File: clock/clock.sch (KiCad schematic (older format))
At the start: 21 parts

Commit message: Selected to use the LPC804 over the PIC18F45k20
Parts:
- removed U?: PIC18F45K50_QFP, Package_QFP:TQFP-44_10x10mm_P0.8mm, symbol MCU_Microchip_PIC18:PIC18F45K50_QFP
- added D? (x72): LED, symbol Device:LED
- added R? (x72): 0, symbol Device:R_Small_US
- added U?: LPC804-TSSOP24, symbol MCU_NXP_LPC804:LPC804-TSSOP24
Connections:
- net labels added: GND, ~OE
- wire segments 17 -> 110
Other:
- note added: "Shift Register"
- note removed: "Almost the correct processor"
- note removed: "Shift Register (Add LEDs)"

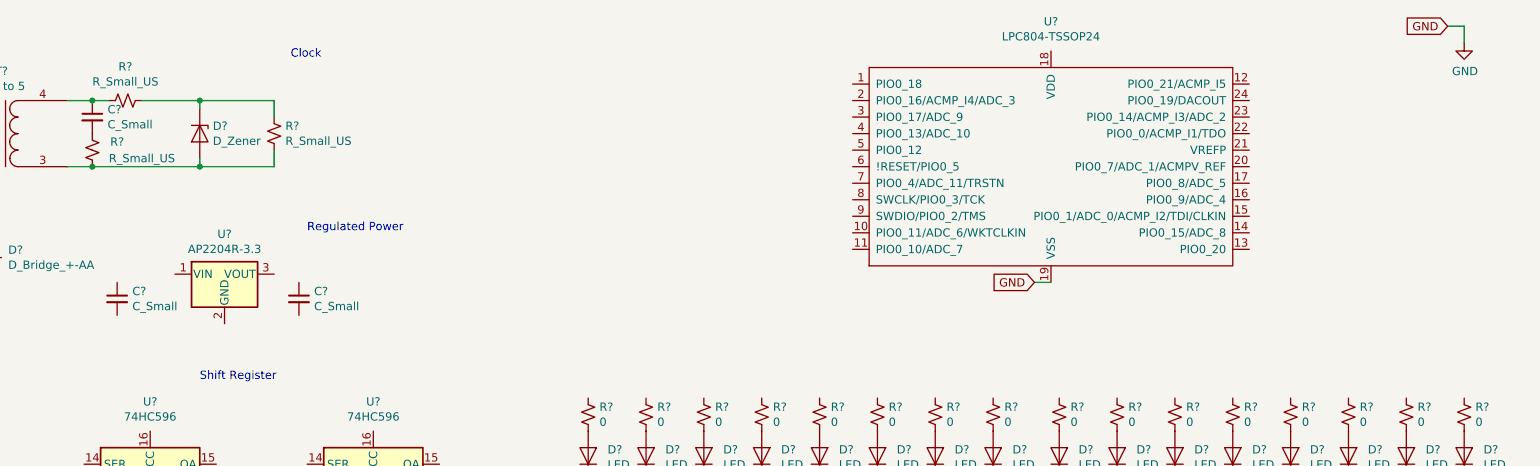
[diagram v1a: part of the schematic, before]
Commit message: Selecting serial data lines impressed the importance of selecting appropriate pins for my cap touch
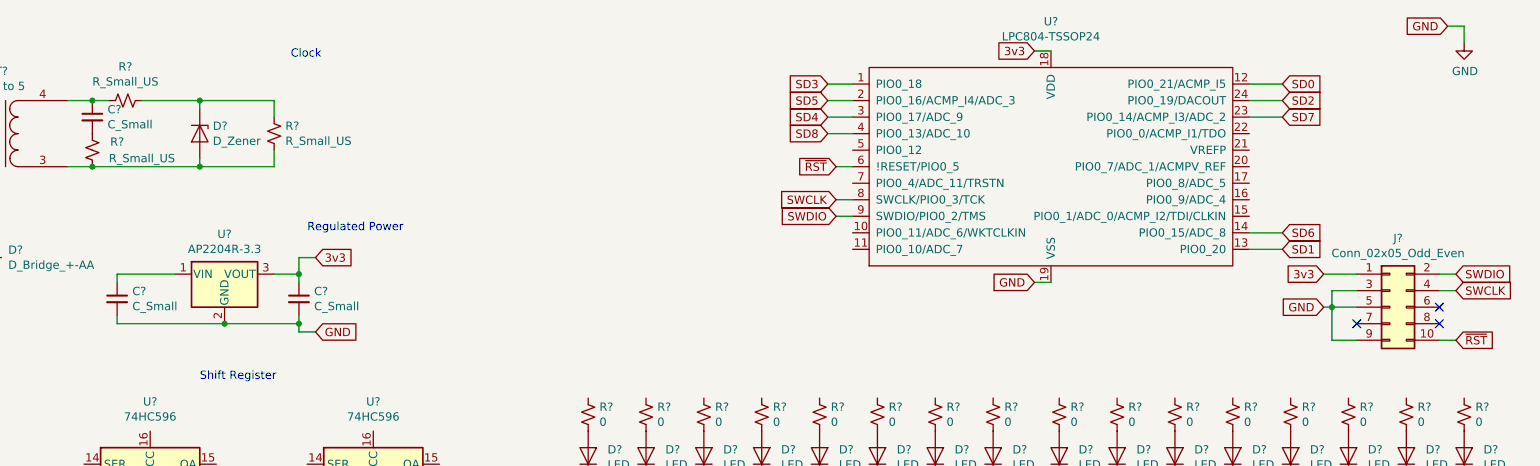
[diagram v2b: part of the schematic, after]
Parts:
- added J?: Conn_02x05_Odd_Even, symbol Connector_Generic:Conn_02x05_Odd_Even
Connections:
- net GND: now also C?.2, C?.2, U?.2 (GND), J?.3 (Pin_3), J?.5 (Pin_5), J?.9 (Pin_9)
- net at U?.1 (VIN): now also C?.1
- net 3v3: now reaches U?.3 (VOUT)
- net 3v3: now also C?.1, U?.18 (VDD), J?.1 (Pin_1)
- net SD3: now reaches U?.1 (PIO0_18)
- net SD0: now reaches U?.12 (PIO0_21/ACMP_I5)
- net SD1: now reaches U?.13 (PIO0_20)
- net SD6: now reaches U?.14 (PIO0_15/ADC_8)
- net SD5: now reaches U?.2 (PIO0_16/ACMP_I4/ADC_3)
- net SD7: now reaches U?.23 (PIO0_14/ACMP_I3/ADC_2)
- net SD2: now reaches U?.24 (PIO0_19/DACOUT)
- net SD4: now reaches U?.3 (PIO0_17/ADC_9)
- net SD8: now reaches U?.4 (PIO0_13/ADC_10)
- net ~RST: now reaches U?.6 (!RESET/PIO0_5)
- net ~RST: now also J?.10 (Pin_10)
- net SWCLK: now reaches U?.8 (SWCLK/PIO0_3/TCK)
- net SWCLK: now also J?.4 (Pin_4)
- net SWDIO: now reaches U?.9 (SWDIO/PIO0_2/TMS)
- net SWDIO: now also J?.2 (Pin_2)
- no-connect marks 0 -> 3
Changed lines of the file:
@@
 Wire Wire Line
 	8350 2150 8450 2150
+$Comp
+L Connector_Generic:Conn_02x05_Odd_Even J?
+U 1 1 5E00183C
+P 10500 2300
+F 0 "J?" H 10550 2717 50  0000 C CNN
+F 1 "Conn_02x05_Odd_Even" H 10550 2626 50  0000 C CNN
+F 2 "" H 10500 2300 50  0001 C CNN
+F 3 "~" H 10500 2300 50  0001 C CNN
+	1    10500 2300
+	1    0    0    -1
+$EndComp
+Text GLabel 10100 2100 0    50   Input ~ 0
+3v3
+Wire Wire Line
+	10100 2100 10300 2100
+Text GLabel 10100 2300 0    50   Input ~ 0
+GND
+Wire Wire Line
+	10300 2200 10150 2200
+Wire Wire Line
+	10150 2200 10150 2300
+Wire Wire Line
+	10150 2300 10100 2300
+Wire Wire Line
+	10300 2300 10150 2300
+Connection ~ 10150 2300
+Wire Wire Line
+	10300 2500 10150 2500
+Wire Wire Line
+	10150 2500 10150 2300
+NoConn ~ 10300 2400
+NoConn ~ 10800 2400
+NoConn ~ 10800 2300
+Text GLabel 10900 2500 2    50   Input ~ 0
+~RST
+Text GLabel 10900 2200 2    50   Input ~ 0
+SWCLK
+Text GLabel 10900 2100 2    50   Input ~ 0
+SWDIO
+Wire Wire Line
+	10800 2100 10900 2100
+Wire Wire Line
+	10800 2200 10900 2200
+Wire Wire Line
+	10800 2500 10900 2500
+Text GLabel 7150 1750 0    50   Input ~ 0
+SWDIO
+Text GLabel 7150 1650 0    50   Input ~ 0
+SWCLK
+Wire Wire Line
+	7150 1650 7250 1650
+Wire Wire Line
+	7150 1750 7250 1750
+Text GLabel 7150 1450 0    50   Input ~ 0
+~RST
+Wire Wire Line
+	7150 1450 7250 1450
+Text GLabel 8350 750  0    50   Input ~ 0
+3v3
+Wire Wire Line
+	8350 750  8450 750
+Wire Wire Line
+	3750 2100 3900 2100
+Wire Wire Line
+	3900 2100 3900 2150
+Wire Wire Line
+	2800 2150 2800 2100
+Wire Wire Line
+	2800 2100 3150 2100
+Wire Wire Line
+	2800 2350 2800 2400
+Wire Wire Line
+	2800 2400 3450 2400
+Wire Wire Line
+	3900 2400 3900 2350
+Connection ~ 3450 2400
+Wire Wire Line
+	3450 2400 3900 2400
+Text GLabel 4000 2000 2    50   Input ~ 0
+3v3
+Text GLabel 4000 2450 2    50   Input ~ 0
+GND
+Wire Wire Line
+	4000 2000 3900 2000
+Wire Wire Line
+	3900 2000 3900 2100
+Connection ~ 3900 2100
+Wire Wire Line
+	4000 2450 3900 2450
+Wire Wire Line
+	3900 2450 3900 2400
+Connection ~ 3900 2400
+Text GLabel 9850 950  2    50   Input ~ 0
+SD0
+Text GLabel 9850 1950 2    50   Input ~ 0
+SD1
+Text GLabel 9850 1050 2    50   Input ~ 0
+SD2
+Text GLabel 7100 950  0    50   Input ~ 0
+SD3
+Text GLabel 7100 1150 0    50   Input ~ 0
+SD4
+Text GLabel 7100 1050 0    50   Input ~ 0
+SD5
+Text GLabel 9850 1850 2    50   Input ~ 0
+SD6
+Text GLabel 9850 1150 2    50   Input ~ 0
+SD7
+Text GLabel 7100 1250 0    50   Input ~ 0
+SD8
+Wire Wire Line
+	9650 950  9850 950
+Wire Wire Line
+	9650 1050 9850 1050
+Wire Wire Line
+	9650 1150 9850 1150
+Wire Wire Line
+	9650 1850 9850 1850
+Wire Wire Line
+	9650 1950 9850 1950
+Wire Wire Line
+	7100 950  7250 950
+Wire Wire Line
+	7100 1050 7250 1050
+Wire Wire Line
+	7100 1150 7250 1150
+Wire Wire Line
+	7100 1250 7250 1250
 $EndSCHEMATC

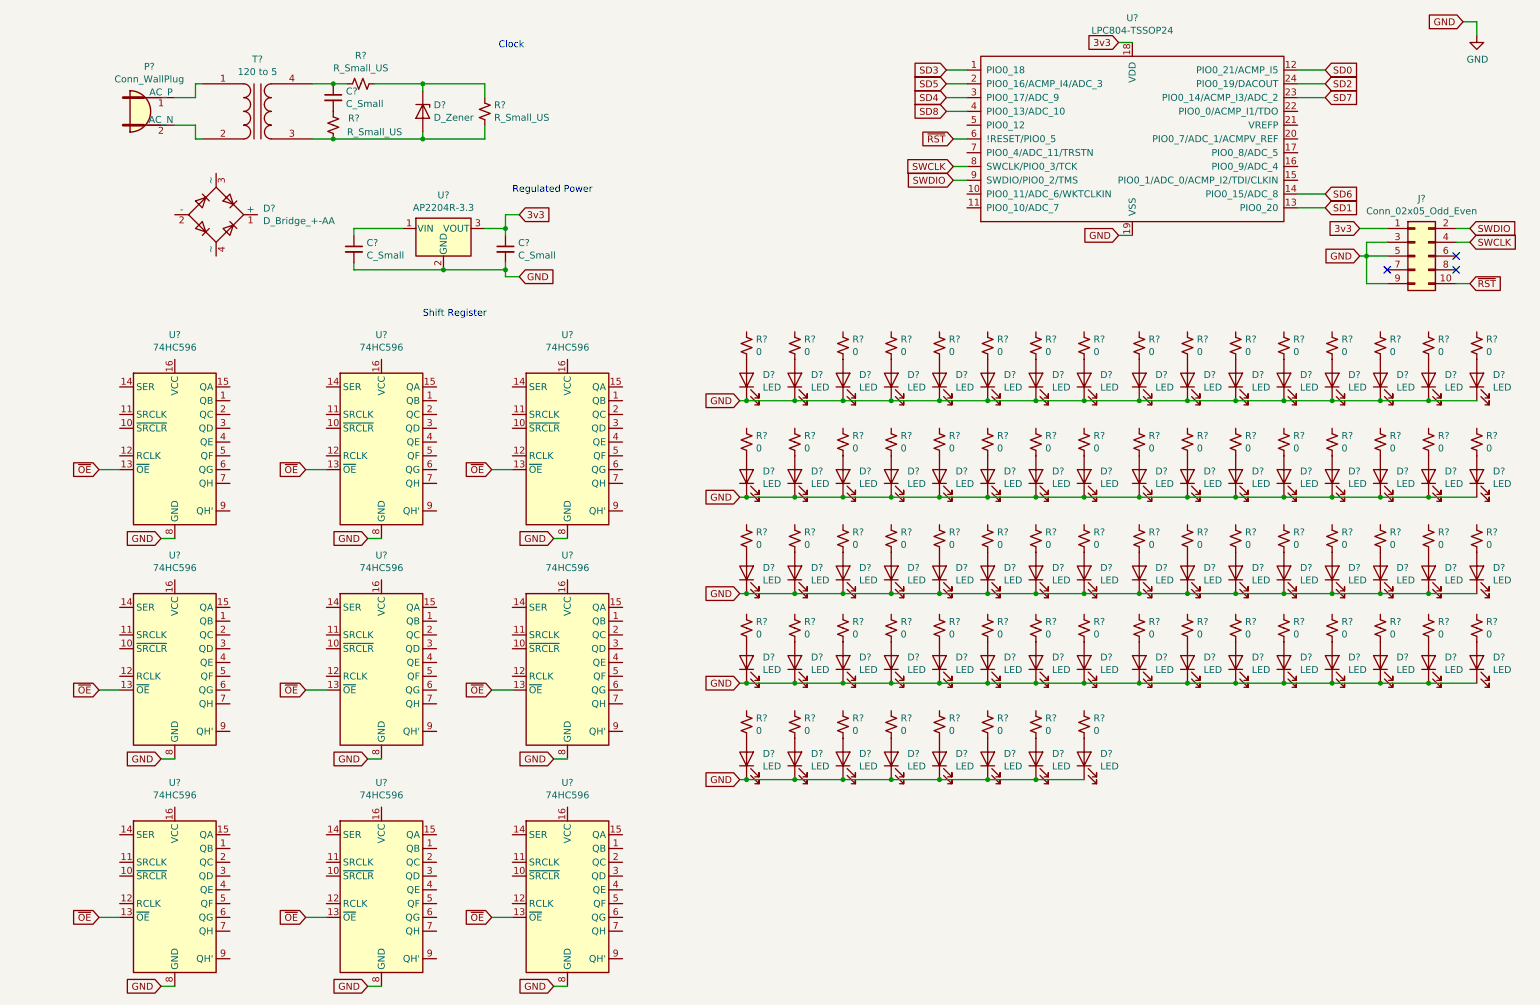
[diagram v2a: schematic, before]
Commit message: Selected 596 shift register. Redid LED schematics. Started bom. Updated readme todo list
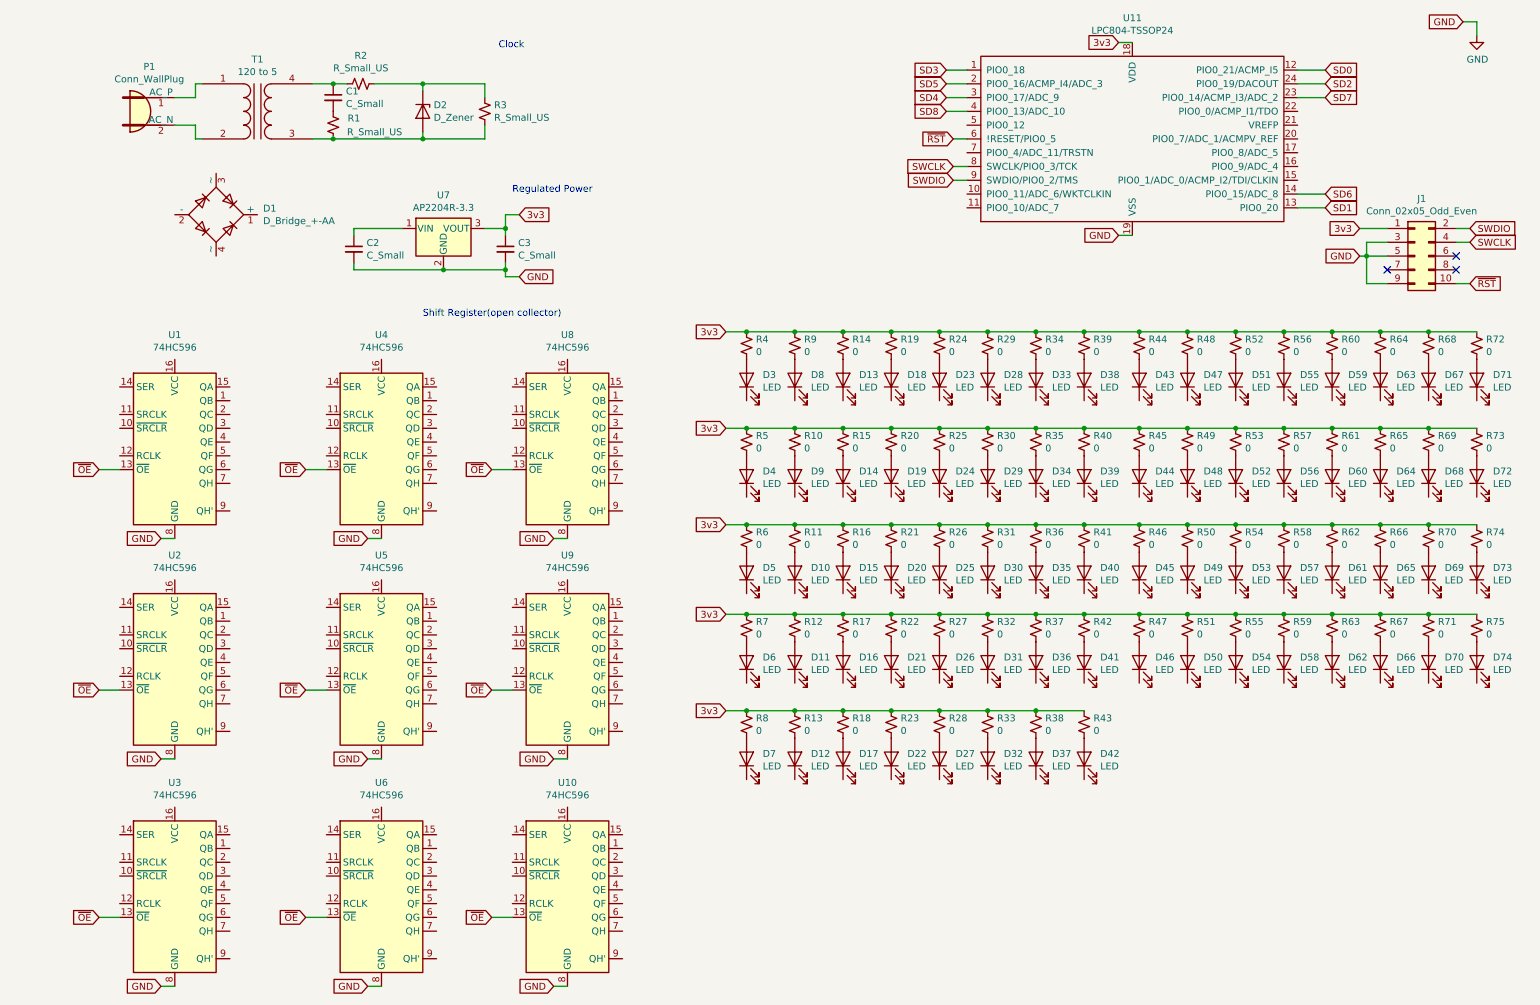
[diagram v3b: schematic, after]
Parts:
- gave numbers to parts that had none: 166
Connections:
- net 3v3: now also R10.1, R11.1, R12.1, R13.1, R14.1, R15.1, R16.1, R17.1, R18.1, R19.1, R20.1, R21.1, R22.1, R23.1, R24.1, R25.1, R26.1, R27.1, R28.1, R29.1, R30.1, R31.1, R32.1, R33.1, R34.1, R35.1, R36.1, R37.1, R38.1, R39.1, R4.1, R40.1, R41.1, R42.1, R43.1, R44.1, R45.1, R46.1, R47.1, R48.1, R49.1, R5.1, R50.1, R51.1, R52.1, R53.1, R54.1, R55.1, R56.1, R57.1, R58.1, R59.1, R6.1, R60.1, R61.1, R62.1, R63.1, R64.1, R65.1, R66.1, R67.1, R68.1, R69.1, R7.1, R70.1, R71.1, R72.1, R73.1, R74.1, R75.1, R8.1, R9.1
- net GND: no longer D10.1 (K), D11.1 (K), D12.1 (K), D13.1 (K), D14.1 (K), D15.1 (K), D16.1 (K), D17.1 (K), D18.1 (K), D19.1 (K), D20.1 (K), D21.1 (K), D22.1 (K), D23.1 (K), D24.1 (K), D25.1 (K), D26.1 (K), D27.1 (K), D28.1 (K), D29.1 (K), D3.1 (K), D30.1 (K), D31.1 (K), D32.1 (K), D33.1 (K), D34.1 (K), D35.1 (K), D36.1 (K), D37.1 (K), D38.1 (K), D39.1 (K), D4.1 (K), D40.1 (K), D41.1 (K), D42.1 (K), D43.1 (K), D44.1 (K), D45.1 (K), D46.1 (K), D47.1 (K), D48.1 (K), D49.1 (K), D5.1 (K), D50.1 (K), D51.1 (K), D52.1 (K), D53.1 (K), D54.1 (K), D55.1 (K), D56.1 (K), D57.1 (K), D58.1 (K), D59.1 (K), D6.1 (K), D60.1 (K), D61.1 (K), D62.1 (K), D63.1 (K), D64.1 (K), D65.1 (K), D66.1 (K), D67.1 (K), D68.1 (K), D69.1 (K), D7.1 (K), D70.1 (K), D71.1 (K), D72.1 (K), D73.1 (K), D74.1 (K), D8.1 (K), D9.1 (K)
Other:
- note added: "Shift Register(open collector)"
- note removed: "Shift Register"

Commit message: Worked on all LED and 596 nets before realizing that I was on the wrong branch. Going to push on branch 191311 and then switch my local back to the master branch
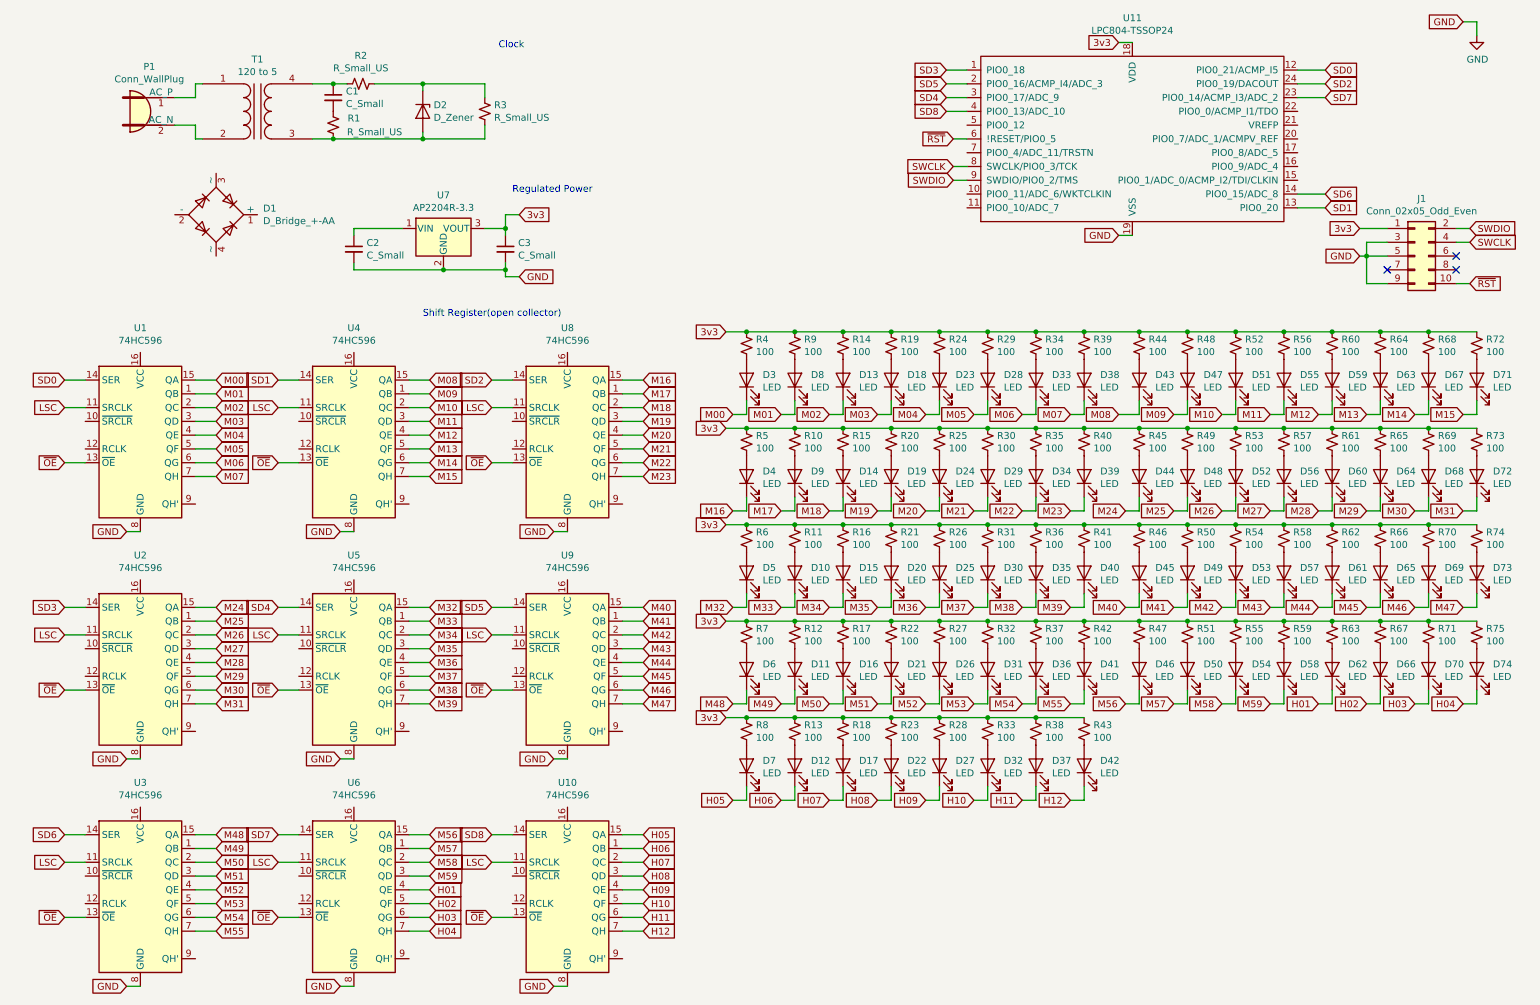
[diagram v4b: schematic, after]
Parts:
- R10, R11, R12, R13, R14, R15, R16, R17, R18, R19, R20, R21, R22, R23, R24, R25, R26, R27, R28, R29, R30, R31, R32, R33, R34, R35, R36, R37, R38, R39, R4, R40, R41, R42, R43, R44, R45, R46, R47, R48, R49, R5, R50, R51, R52, R53, R54, R55, R56, R57, R58, R59, R6, R60, R61, R62, R63, R64, R65, R66, R67, R68, R69, R7, R70, R71, R72, R73, R74, R75, R8, R9: value 0 -> 100
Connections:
- net SD0: now also U1.14 (SER)
- net SD1: now also U4.14 (SER)
- net SD2: now also U8.14 (SER)
- net SD3: now also U2.14 (SER)
- net SD4: now also U5.14 (SER)
- net SD5: now also U9.14 (SER)
- net SD6: now also U3.14 (SER)
- net SD7: now also U6.14 (SER)
- net SD8: now also U10.14 (SER)
- net M01: now reaches U1.1 (QB)
- net M01: now also D8.1 (K)
- net LSC: now reaches U1.11 (SRCLK)
- net LSC: now also U10.11 (SRCLK), U2.11 (SRCLK), U3.11 (SRCLK), U4.11 (SRCLK), U5.11 (SRCLK), U6.11 (SRCLK), U8.11 (SRCLK), U9.11 (SRCLK)
- net M00: now reaches U1.15 (QA)
- net M00: now also D3.1 (K)
- net M02: now reaches U1.2 (QC)
- net M02: now also D13.1 (K)
- net M03: now reaches U1.3 (QD)
- net M03: now also D18.1 (K)
- net M04: now reaches U1.4 (QE)
- net M04: now also D23.1 (K)
- net M05: now reaches U1.5 (QF)
- net M05: now also D28.1 (K)
- net M06: now reaches U1.6 (QG)
- net M06: now also D33.1 (K)
- net M07: now reaches U1.7 (QH)
- net M07: now also D38.1 (K)
- net M09: now reaches U4.1 (QB)
- net M09: now also D47.1 (K)
- net M08: now reaches U4.15 (QA)
- net M08: now also D43.1 (K)
- net M10: now reaches U4.2 (QC)
- net M10: now also D51.1 (K)
- net M11: now reaches U4.3 (QD)
- net M11: now also D55.1 (K)
- net M12: now reaches U4.4 (QE)
- net M12: now also D59.1 (K)
- net M13: now reaches U4.5 (QF)
- net M13: now also D63.1 (K)
- net M14: now reaches U4.6 (QG)
- net M14: now also D67.1 (K)
- net M15: now reaches U4.7 (QH)
- net M15: now also D71.1 (K)
- net M17: now reaches U8.1 (QB)
- net M17: now also D9.1 (K)
- net M16: now reaches U8.15 (QA)
- net M16: now also D4.1 (K)
- net M18: now reaches U8.2 (QC)
- net M18: now also D14.1 (K)
- net M19: now reaches U8.3 (QD)
- net M19: now also D19.1 (K)
- net M20: now reaches U8.4 (QE)
- net M20: now also D24.1 (K)
- net M21: now reaches U8.5 (QF)
- net M21: now also D29.1 (K)
- net M22: now reaches U8.6 (QG)
- net M22: now also D34.1 (K)
- net M23: now reaches U8.7 (QH)
- net M23: now also D39.1 (K)
- net H06: now reaches U10.1 (QB)
- net H06: now also D12.1 (K)
- net H05: now reaches U10.15 (QA)
- net H05: now also D7.1 (K)
- net H07: now reaches U10.2 (QC)
- net H07: now also D17.1 (K)
- net H08: now reaches U10.3 (QD)
- net H08: now also D22.1 (K)
- net H09: now reaches U10.4 (QE)
- net H09: now also D27.1 (K)
- net H10: now reaches U10.5 (QF)
- net H10: now also D32.1 (K)
- net H11: now reaches U10.6 (QG)
- net H11: now also D37.1 (K)
- net H12: now reaches U10.7 (QH)
- net H12: now also D42.1 (K)
- net M25: now reaches U2.1 (QB)
- net M25: now also D48.1 (K)
- net M24: now reaches U2.15 (QA)
- net M24: now also D44.1 (K)
- net M26: now reaches U2.2 (QC)
- net M26: now also D52.1 (K)
- net M27: now reaches U2.3 (QD)
- net M27: now also D56.1 (K)
- net M28: now reaches U2.4 (QE)
- net M28: now also D60.1 (K)
- net M29: now reaches U2.5 (QF)
- net M29: now also D64.1 (K)
- net M30: now reaches U2.6 (QG)
- net M30: now also D68.1 (K)
- net M31: now reaches U2.7 (QH)
- net M31: now also D72.1 (K)
- net M33: now reaches U5.1 (QB)
- net M33: now also D10.1 (K)
- net M32: now reaches U5.15 (QA)
- net M32: now also D5.1 (K)
- net M34: now reaches U5.2 (QC)
- net M34: now also D15.1 (K)
- net M35: now reaches U5.3 (QD)
- net M35: now also D20.1 (K)
- net M36: now reaches U5.4 (QE)
- net M36: now also D25.1 (K)
- net M37: now reaches U5.5 (QF)
- net M37: now also D30.1 (K)
- net M38: now reaches U5.6 (QG)
- net M38: now also D35.1 (K)
- net M39: now reaches U5.7 (QH)
- net M39: now also D40.1 (K)
- net M41: now reaches U9.1 (QB)
- net M41: now also D49.1 (K)
- net M40: now reaches U9.15 (QA)
- net M40: now also D45.1 (K)
- net M42: now reaches U9.2 (QC)
- net M42: now also D53.1 (K)
- net M43: now reaches U9.3 (QD)
- net M43: now also D57.1 (K)
- net M44: now reaches U9.4 (QE)
- net M44: now also D61.1 (K)
- net M45: now reaches U9.5 (QF)
- net M45: now also D65.1 (K)
- net M46: now reaches U9.6 (QG)
- net M46: now also D69.1 (K)
- net M47: now reaches U9.7 (QH)
- net M47: now also D73.1 (K)
- net M57: now reaches U6.1 (QB)
- net M57: now also D50.1 (K)
- net M56: now reaches U6.15 (QA)
- net M56: now also D46.1 (K)
- net M58: now reaches U6.2 (QC)
- net M58: now also D54.1 (K)
- net M59: now reaches U6.3 (QD)
- net M59: now also D58.1 (K)
- net H01: now reaches U6.4 (QE)
- net H01: now also D62.1 (K)
- net H02: now reaches U6.5 (QF)
- net H02: now also D66.1 (K)
- net H03: now reaches U6.6 (QG)
- net H03: now also D70.1 (K)
- net H04: now reaches U6.7 (QH)
- net H04: now also D74.1 (K)
- net M49: now reaches U3.1 (QB)
- net M49: now also D11.1 (K)
- net M48: now reaches U3.15 (QA)
- net M48: now also D6.1 (K)
- net M50: now reaches U3.2 (QC)
- net M50: now also D16.1 (K)
- net M51: now reaches U3.3 (QD)
- net M51: now also D21.1 (K)
- net M52: now reaches U3.4 (QE)
- net M52: now also D26.1 (K)
- net M53: now reaches U3.5 (QF)
- net M53: now also D31.1 (K)
- net M54: now reaches U3.6 (QG)
- net M54: now also D36.1 (K)
- net M55: now reaches U3.7 (QH)
- net M55: now also D41.1 (K)
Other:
- moved on the sheet: D11, D12, D16, D17, D21, D22, D26, D27, D31, D32, D36, D37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
